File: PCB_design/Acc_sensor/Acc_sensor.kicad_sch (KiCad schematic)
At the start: 61 parts, among them J1 Conn_01x04_Socket, J2 Conn_01x04_Pin, J3 USB_C_Receptacle_USB2.0_16P, Q1 NMOS, Q2 NMOS, SW1 SW_SPST, SW2 SW_SPST, SW3 SW_SPST, U1 ESP32-C3, U2 LIS2DE12, U3 DW01A, U3 MAX17263xxTE, U5 TPS22917LDBV, U7 TLV75533PDBV, Y1 Crystal_GND24

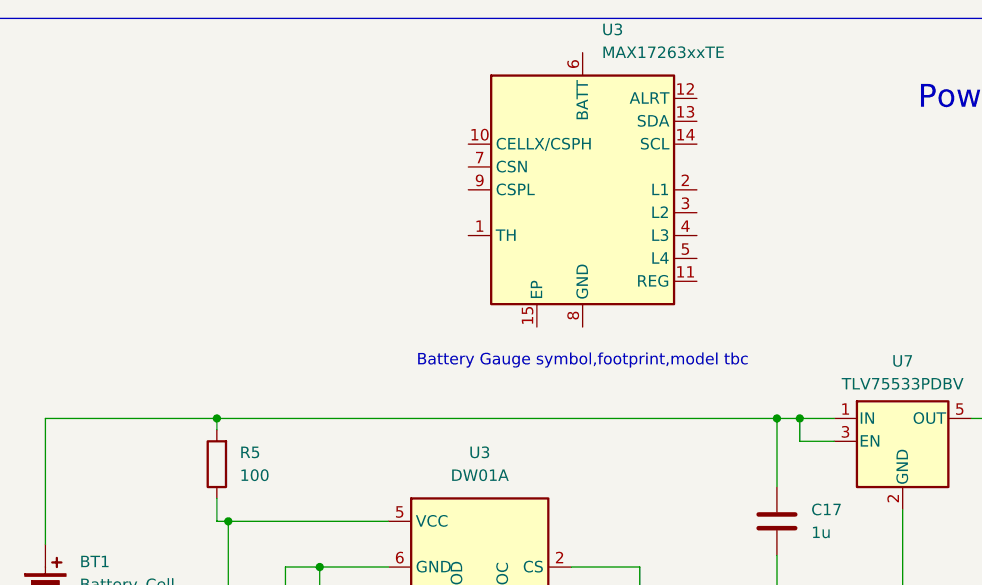
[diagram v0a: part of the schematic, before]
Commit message: update
choose a appropriate fuel gauge and draw the correspond symbol to add it into power management system for both two pcb file
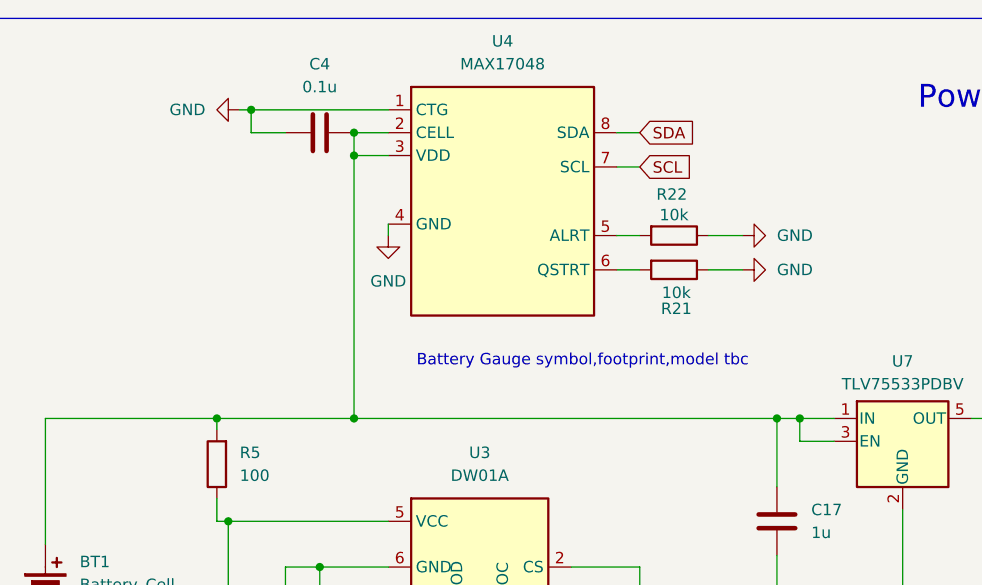
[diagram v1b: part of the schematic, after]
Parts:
- removed U3: MAX17263xxTE, Package_DFN_QFN:DFN-14-1EP_3x3mm_P0.4mm_EP1.78x2.35mm, symbol Battery_Management:MAX17263xxTE
- added C4: 0.1u, symbol Device:C
- added R21, R22: 10k, symbol Device:R
- added U4: MAX17048, Package_DFN_QFN:TDFN-8-1EP_2x2mm_P0.5mm_EP0.8x1.2mm, symbol symlib:MAX17048
- Y1: footprint (none) -> Crystal:Crystal_SMD_SeikoEpson_TSX3225-4Pin_3.2x2.5mm_HandSoldering
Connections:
- net GND: now also C4.1, R21.1, R22.1, U4.1 (CTG), U4.4 (GND)
- net SCL: now also U4.7 (SCL)
- net SDA: now also U4.8 (SDA)
- net at BT1.1 (+), C17.1, R5.2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: now also C4.2, U4.2 (CELL), U4.3 (VDD)
- new net: R21.2, U4.6 (QSTRT)
- new net: R22.2, U4.5 (ALRT)

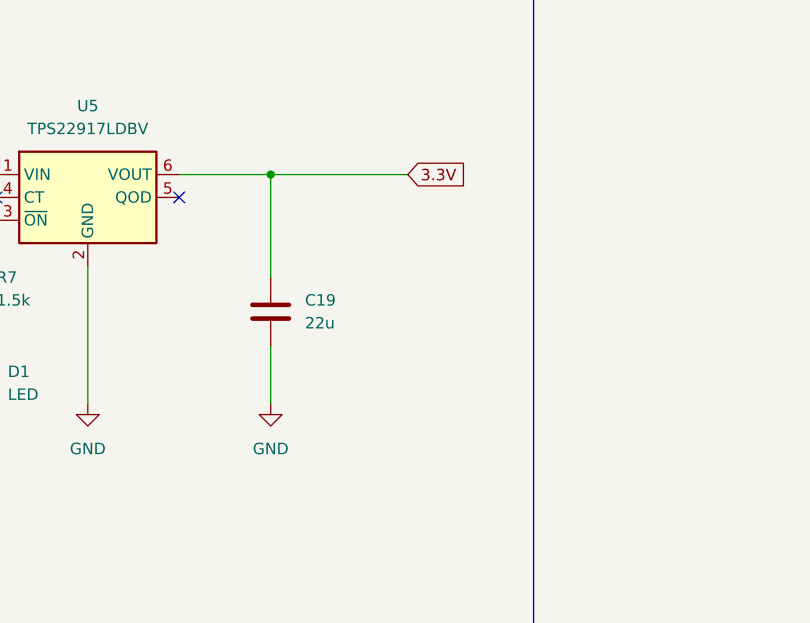
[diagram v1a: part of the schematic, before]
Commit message: update
add the ceramic parallel capacitor for driving ESP32 at big current
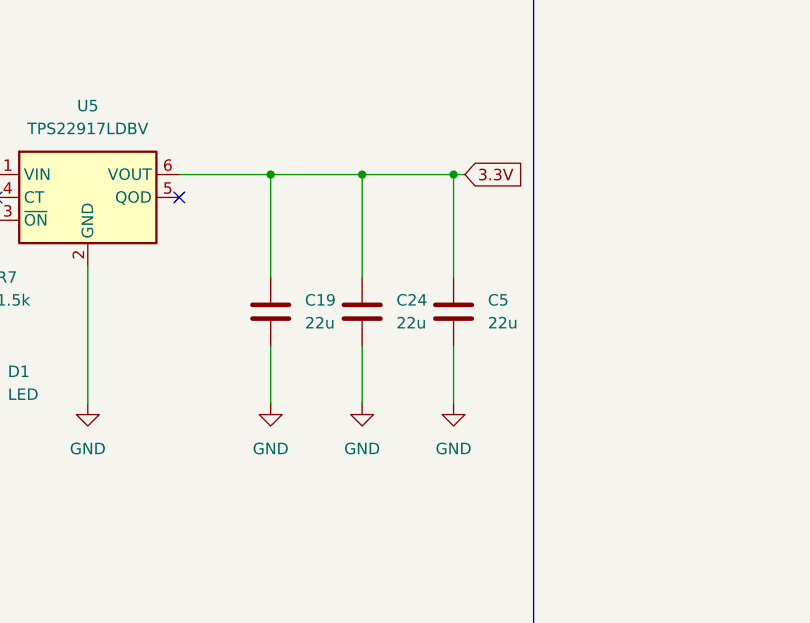
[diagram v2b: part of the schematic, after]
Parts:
- added C24, C5: 22u, symbol Device:C
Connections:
- net 3.3V: now also C24.1, C5.1
- net GND: now also C24.2, C5.2

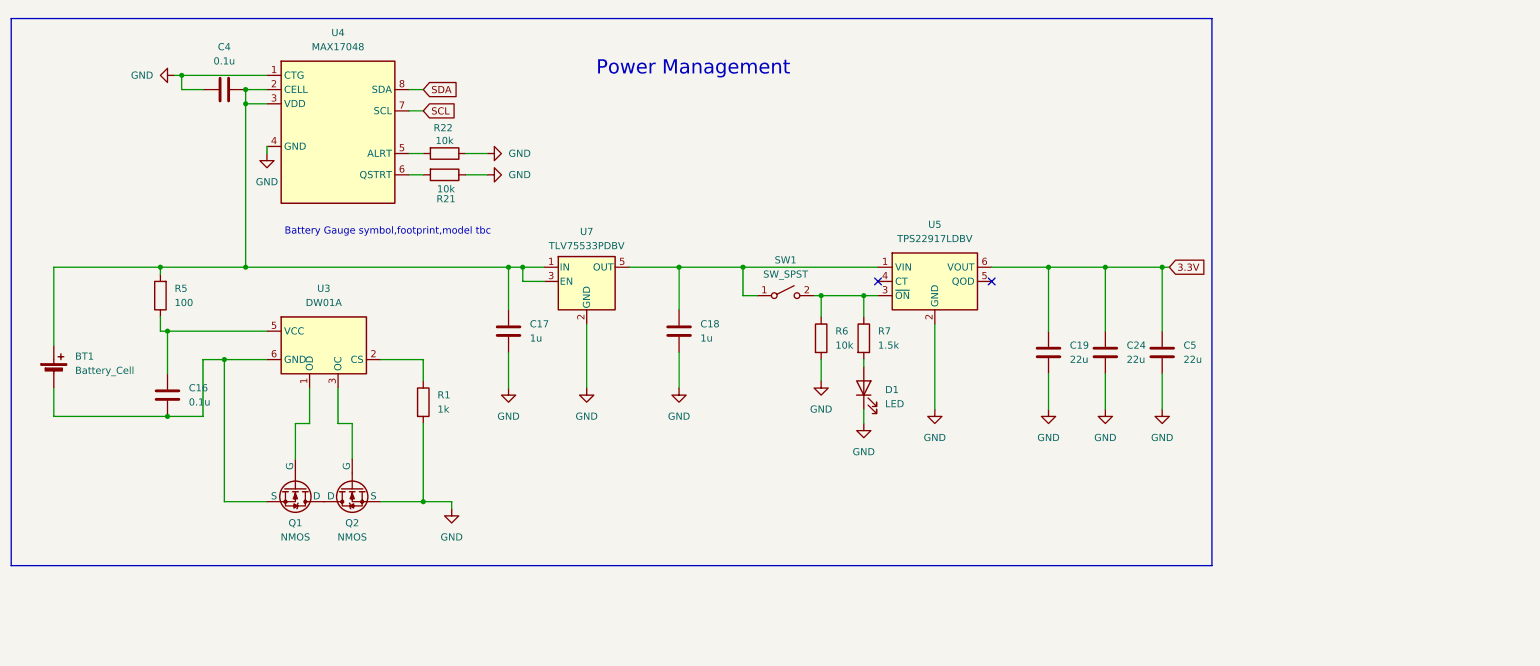
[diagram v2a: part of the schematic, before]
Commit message: applied LTC4412 to both file
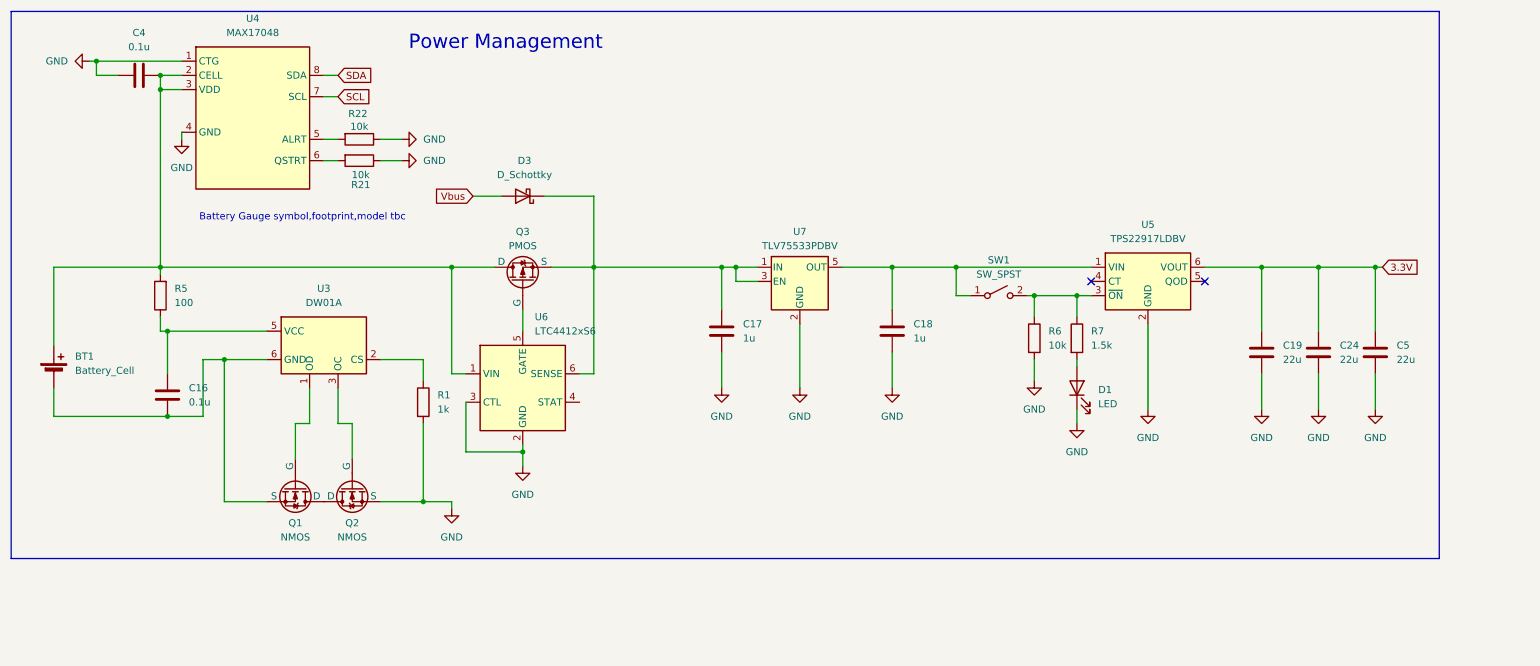
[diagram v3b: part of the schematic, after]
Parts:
- added D3: D_Schottky, symbol Device:D_Schottky
- added Q3: PMOS, symbol Simulation_SPICE:PMOS
- added U6: LTC4412xS6, Package_TO_SOT_SMD:TSOT-23-6, symbol Power_Management:LTC4412xS6
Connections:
- net GND: now also U6.2 (GND), U6.3 (CTL)
- net Vbus: now also D3.2 (A)
- net at BT1.1 (+), C4.2, R5.2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: now also Q3.1 (D), U6.1 (VIN); no longer C17.1, U7.1 (IN), U7.3 (EN)
- new net: C17.1, D3.1 (K), Q3.3 (S), U6.6 (SENSE), U7.1 (IN), U7.3 (EN)
- new net: Q3.2 (G), U6.5 (GATE)
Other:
- moved on the sheet: C17, C18, C19, C24, C4, C5, D1, R21, R22, R6, R7, SW1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

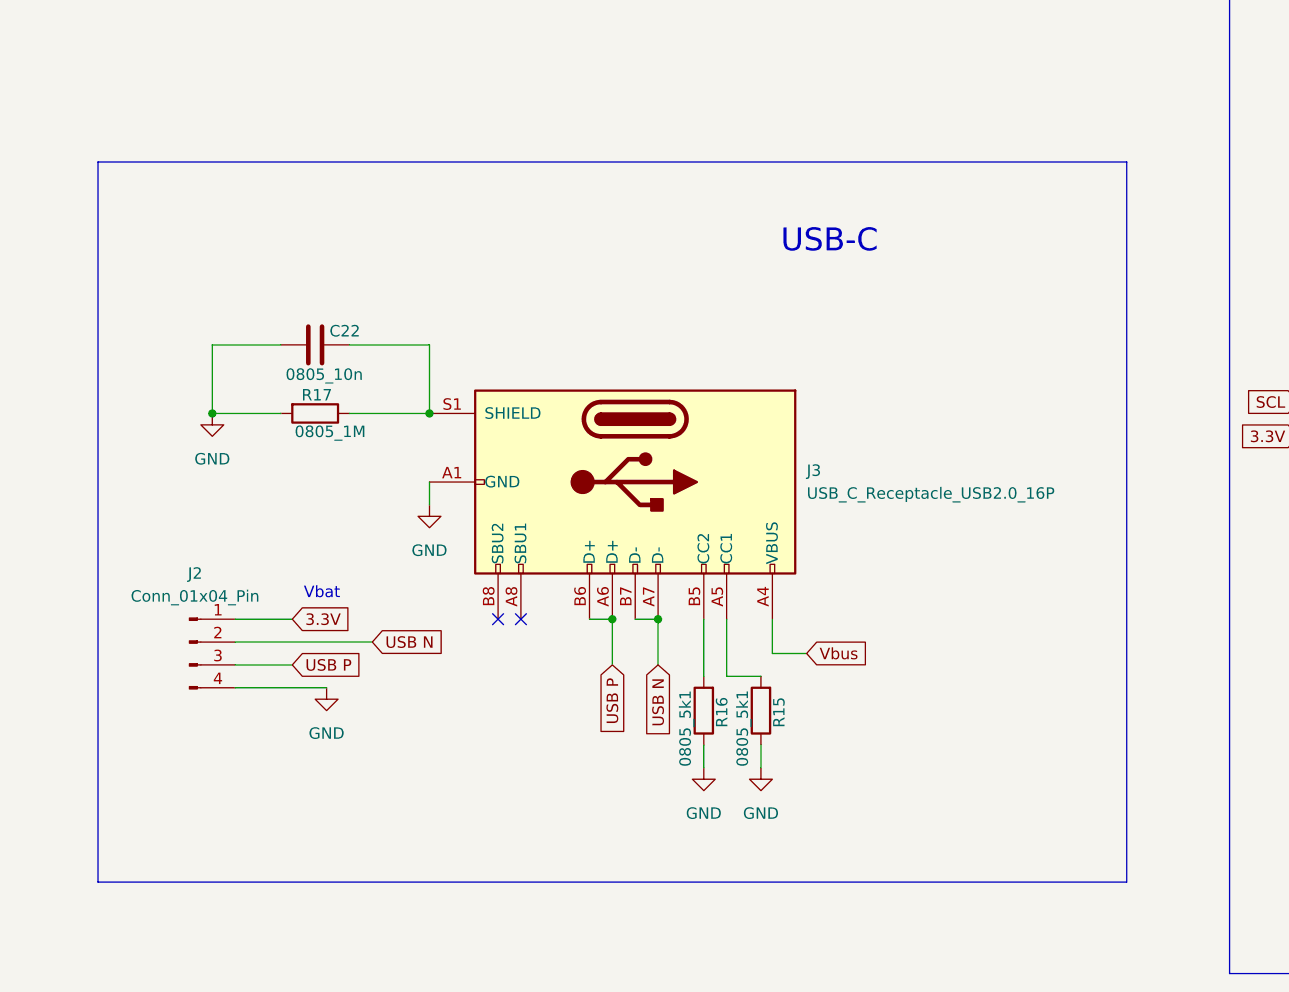
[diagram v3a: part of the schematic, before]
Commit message: quick update
split USBC into an individual file
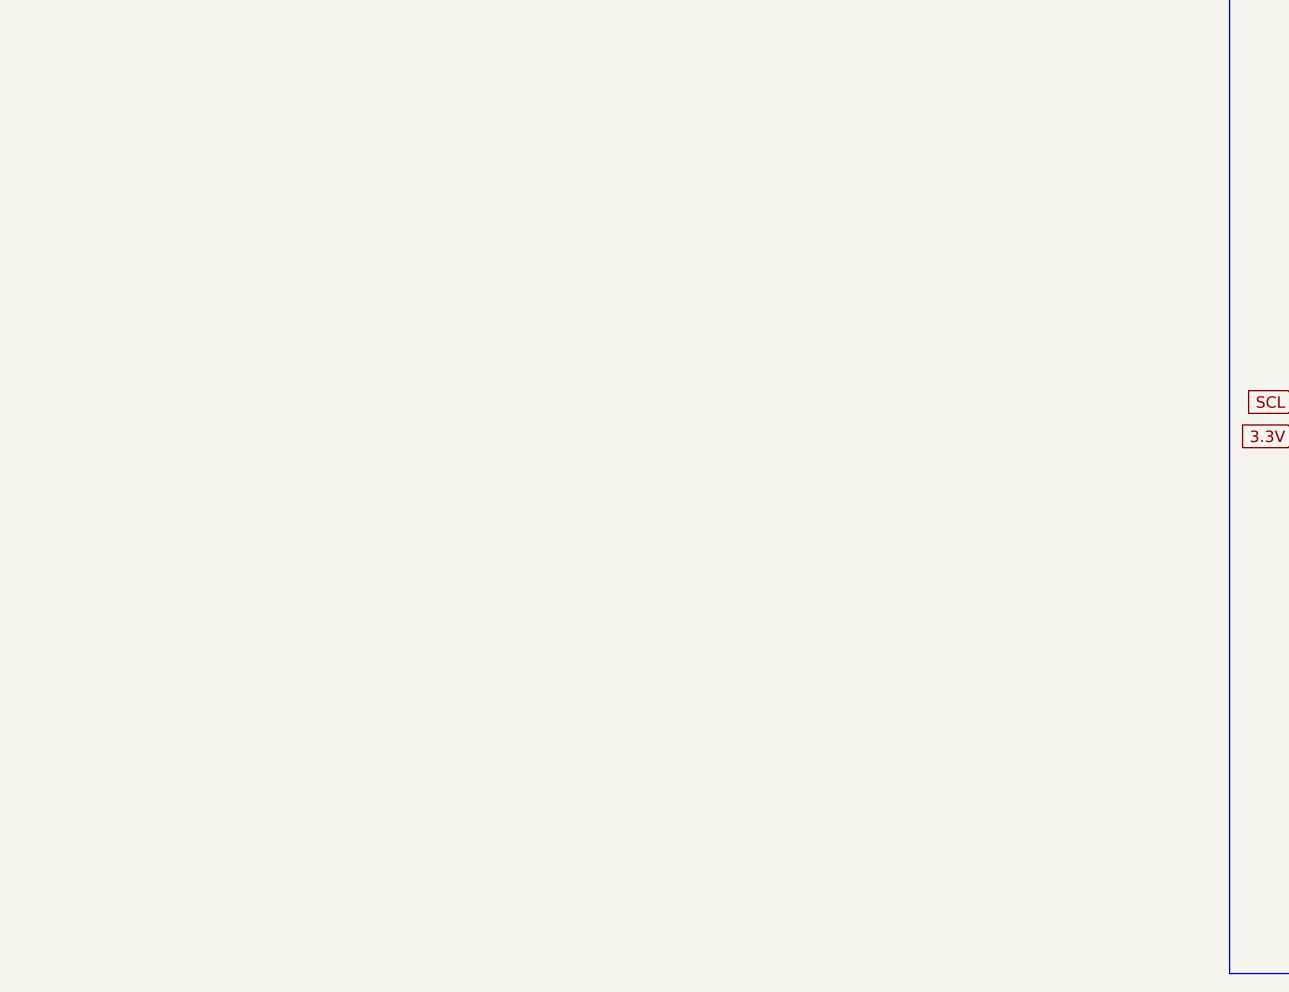
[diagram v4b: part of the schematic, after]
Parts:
- removed C22: 0805_10n, symbol Device:C
- removed J2: Conn_01x04_Pin, symbol Connector:Conn_01x04_Pin
- removed J3: USB_C_Receptacle_USB2.0_16P, symbol Connector:USB_C_Receptacle_USB2.0_16P
- removed R15, R16: 0805_5k1, symbol Device:R
- removed R17: 0805_1M, symbol Device:R
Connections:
- no-connect marks 6 -> 4
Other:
- note removed: "USB-C"

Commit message: 11
1
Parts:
- AE1: footprint customfootprint:Chip Antenna ANT2012 -> Custom footprint:Chip Antenna 2450AT18A100
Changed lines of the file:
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@@
 			)
 		)
-		(property "Footprint" "customfootprint:Chip Antenna ANT2012"
+		(property "Footprint" "Custom footprint:Chip Antenna 2450AT18A100"
 			(at 356.235 186.69 0)
 			(effects
